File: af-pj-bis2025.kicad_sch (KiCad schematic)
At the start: 59 parts, among them IC1 ADS127L14IRSHT, IC2 OPA210IDBVR, IC3 REF6225IDGKR, IC4 TPS7A4700RGWR, IC5 TPS7A4700RGWR, U1 MIC5237-5.0YU, U2 ALD114904ASAL, U3 OPA380AID, U4 OPA380AID

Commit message: ADC追加
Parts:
- removed C1, C3, C8, C9: 3.18nF, symbol Device:C
- removed C4, C5: C, symbol Device:C
- removed IC1: ADS127L14IRSHT, QFN40P700X700X100-57N-D, symbol SamacSys_Parts:ADS127L14IRSHT
- removed IC2: OPA210IDBVR, SOT95P280X145-5N, symbol SamacSys_Parts:OPA210IDBVR
- removed IC3: REF6225IDGKR, SOP65P490X110-8N, symbol SamacSys_Parts:REF6225IDGKR
- removed IC4, IC5: TPS7A4700RGWR, QFN65P500X500X100-21N-D, symbol SamacSys_Parts:TPS7A4700RGWR
- removed R10: 0.047, symbol Device:R
- removed R11, R13, R14, R17, R18, R9: 0, symbol Device:R
- removed R12, R16: 0.1, symbol Device:R
- removed R15, R7: 100k, symbol Device:R
- removed R3, R4: R, symbol Device:R
- removed R5: 1.00k, symbol Device:R
- removed R6: 37.4, symbol Device:R
- removed R8: 120k, symbol Device:R
- removed Re1, Re2, Re3, Re4: 50kΩ, symbol Device:R
- removed U1: MIC5237-5.0YU, TO-263-3_MCL, symbol MIC5237-5.0YU:MIC5237-5.0YU
- removed U2: ALD114904ASAL, 8-SOIC_ALD, symbol ALD114904ASAL:ALD114904ASAL
- removed U3, U4: OPA380AID, D8, symbol OPA380:OPA380AID
- added C29: 1n, symbol Device:C
- added C30, C35, C36: 0.1u, symbol Device:C
- added C31, C32: 270p, symbol Device:C
- added C33: 22n, symbol Device:C
- added C34: 3.18n, symbol Device:C
- added Re10, Re20, Re21, Re24, Re25, Re7, Re8, Re9: 1.2k, symbol Device:R
- added Re11, Re12, Re26, Re27: 5, symbol Device:R
- added Re13, Re14, Re28, Re29: 10, symbol Device:R
- added Re15, Re16, Re17, Re18, Re19: 47, symbol Device:R
- added Re22, Re23, Re5, Re6: 330, symbol Device:R
- added Re30, Re32: 50k, symbol Device:R
- added Re31, Re33: 50k_throughhole, symbol Device:R
- added U1: MIC5237-5.0YU, TO-263-3_MCL, symbol pj-bis2025:MIC5237-5.0YU
- added U10, U7: THS4552IPWR, PW0016A_N, symbol Triac_Thyristor:THS4552IPWR
- added U11: OPA2380AIDGKR, DGK8, symbol pj-bis2025:OPA2380AIDGKR
- added U12: ALD114904APAL, 8-PDIP_ALD, symbol pj-bis2025:ALD114904APAL
- added U5: ADS1220IPW, PW16, symbol Triac_Thyristor:ADS1220IPW
- added U6: UA78L06ACPK, PK0003A_N, symbol Triac_Thyristor:UA78L06ACPK
- added U8: REF5050IDR, D8, symbol Triac_Thyristor:REF5050IDR
- added U9: LT1991ACMS-TRPBF, MSOP-10_MS_LIT, symbol Triac_Thyristor:LT1991ACMS-TRPBF
- C10: value 1u -> 470p
- C11: value 0.033u -> 270p
- C12: value 100 n -> 270p
- C13: value 10u -> 1n
- C14: value 1u -> 22n
- C15: value 47u -> 0.1u
- C16, C17: value 10u -> 0.1u
- C18: value 1u -> 0.1u
- C19: value 22u -> 0.1u
- C20: value 10u -> 3.18n
- C21: value 1u -> 3.18n
- C22: value 22u -> 3.18n
- C23: value C -> 0.33u
- C24, C26, C27: value C -> 0.1u
- C25: value C -> 1u
- C28: value C -> 470p
- R1: value 1.00 k -> 100k
- R2: value 4.99k -> 100k
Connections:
- net 5V is gone; now on net AVDD_5V: C6.1
- net IOVDD is gone; now on net DC_9V: C23.1
- net REFP is gone; now on net AVSS: C26.2
- net VCOM is gone; now on an unnamed net: C13.1
- net AVSS: now also C15.2, C17.1, C18.1, C19.1, C2.2, C21.1, C22.1, C23.2, C27.1, C6.2, C7.2, C30.1, C35.1, C36.1, Re21.1, Re8.1, U1.2 (GND), U1.4, U10.12 (VS-), U11.4 (V-), U12.4 (S12), U12.5 (V-), U5.5 (AVSS), U5.8 (REFN0), U6.2 (COMMON), U7.16 (VS-), U8.4 (GND), U9.3 (P9), U9.4 (VEE); no longer C10.2, C12.1, C13.2, C14.2, C16.2, C26.1, C27.2
- net GND: now also U5.3 (CLK); no longer C17.2, C18.2, C2.2, C20.2, C21.2, C23.2, C28.2, C6.2, C7.2
- net OUT1: now also C22.2, Re31.1, Re32.2, Re7.1
- net OUT2: now also C21.2, Re20.1, Re30.2, Re33.1
- net AIN1P: now reaches C14.1
- net AIN1P: now also Re14.2, U5.11 (AIN0/REFP1)
- net at C28.1: now also Re21.2, Re23.1, Re25.1
- net at C19.2: now also R1.2, U11.3 (INA+)
- net at C10.1: now also Re10.1, Re6.1, Re8.2; no longer R1.2
- net at R2.2: now also C35.2, U11.5 (INB+)
- net at C11.1: now also Re12.1, U7.14 (VOUT1+)
- net at C11.2: now also Re6.2, U7.3 (VIN1-); no longer R2.1
- net +2V5 renamed AVDD_5V
- net AVDD_5V: now also C17.2, C18.2, C36.2, U1.3 (OUT), U10.5 (PD2_N), U10.9 (VS2+), U11.8 (V+), U5.12 (AVDD), U7.1 (PD1_N), U7.13 (VS1+)
- net +6V: no longer names the net of C20.1
- net +6V: now also Re32.1, U11.1 (OUTA); no longer C17.1
- net +9V renamed DC_9V
- net DC_9V: now also U1.1 (IN), U6.3 (INPUT)
- removed net AVDD: C12.2, C16.1, C24.1, C25.1
- net VCM renamed VREF_0.5V
- net VREF_0.5V: now also R2.1, U9.10 (M1), U9.6 (OUT), U9.8 (M9), U9.9 (M3)
- new net: C10.2, Re5.1, Re7.2, Re9.1
- new net: C12.2, C13.2, Re5.2, U7.2 (VIN1+)
- new net: C27.2, U7.4 (VOCM1)
- new net: Re10.2, Re12.2, Re14.1
- new net: Re17.2, U5.16 (DIN)
- new net: C28.2, Re20.2, Re22.1, Re24.1
- new net: C32.1, Re27.1, U10.10 (VOUT2+)
- new net: Re25.2, Re27.2, Re29.1
- new net: Re18.1, U5.15 (DOUT/*DRDY)
- new net: C29.2, C31.2, Re22.2, U10.6 (VIN2+)
- new net: Re24.2, Re26.2, Re28.1
- new net: Re15.2, U5.2 (*CS)
- new net: C25.1, U8.5 (TRIM/NR)
- new net: C31.1, Re26.1, U10.11 (VOUT2-)
- new net: C34.1, Re30.1, U11.7 (OUTB)
- new net: C30.2, U10.8 (VOCM2)
- new net: C29.1, C32.2, Re23.2, U10.7 (VIN2-)
- new net: C20.2, Re31.2, U11.2 (INA-), U12.3 (DN1)
- new net: Re11.2, Re13.1, Re9.2
- new net: C12.1, Re11.1, U7.15 (VOUT1-)
- new net: C34.2, Re33.2, U11.6 (INB-), U12.6 (DN2)
- new net: Re16.2, U5.1 (SCLK)
- new net: Re19.1, U5.14 (*DRDY)
- new net AIN1N: C14.2, Re13.2, U5.10 (AIN1)
- new net AIN2N: C33.2, Re28.2, U5.6 (AIN3/REFN1)
- new net AIN2P: C33.1, Re29.2, U5.7 (AIN2)
- new net AVDD_6.2V: C24.1, U6.1 (OUTPUT), U8.2 (VIN)
- new net AVDD_6V: C26.1, U9.7 (VCC)
- new net CS*: Re15.1
- new net DIN: Re17.1
- new net DOUT: Re18.2
- new net DRDY: Re19.2
- new net DVDD: C16.1, U5.13 (DVDD)
- new net DVSS: C16.2, U5.4 (DGND)
- new net GATE1: U12.2 (GN1)
- new net GATE2: U12.7 (GN2)
- new net SCLK: Re16.1
- new net VREF_5V: U5.9 (REFP0), U8.6 (VOUT), U9.1 (P1), U9.5 (REF)
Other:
- moved on the sheet: C2, C6, C7

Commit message: ERCを解消した1
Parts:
- removed U10, U7: THS4552IPWR, PW0016A_N, symbol Triac_Thyristor:THS4552IPWR
- added U2: THS4552IPWR, PW0016A_N, symbol pj-bis2025:THS4552IPWR
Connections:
- net AVDD_6V is gone; now on net AVDD_6.2V: C26.1, U9.7 (VCC)
- net AVDD_5V: now also U2.1 (PD1_N), U2.13 (VS1+), U2.5 (PD2_N), U2.9 (VS2+)
- net AVSS: now also U2.12 (VS-), U2.16 (VS-)
- net at C11.1, Re12.1: now also U2.14 (VOUT1+)
- net at C11.2, C13.1, Re6.2: now also U2.3 (VIN1-)
- net at C12.2, C13.2, Re5.2: now also U2.2 (VIN1+)
- net at C27.2: now also U2.4 (VOCM1)
- net at C32.1, Re27.1: now also U2.10 (VOUT2+)
- net at C29.2, C31.2, Re22.2: now also U2.6 (VIN2+)
- net at C31.1, Re26.1: now also U2.11 (VOUT2-)
- net at C30.2: now also U2.8 (VOCM2)
- net at C29.1, C32.2, Re23.2: now also U2.7 (VIN2-)
- net at C12.1, Re11.1: now also U2.15 (VOUT1-)
- no-connect marks 0 -> 1

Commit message: ERCエラー修正2
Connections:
- net GND is gone; now on net AVSS: U5.3 (CLK)
- no-connect marks 1 -> 7
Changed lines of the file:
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@@
 	)
 	(no_connect
+		(at -25.4 295.91)
+	)
+	(no_connect
+		(at 393.7 269.24)
+	)
+	(no_connect
+		(at 30.48 295.91)
+	)
+	(no_connect
+		(at 393.7 264.16)
+	)
+	(no_connect
+		(at 459.74 266.7)
+	)
+	(no_connect
 		(at 482.6 266.7)
 	)
+	(no_connect
+		(at 459.74 264.16)
+	)
 	(wire
 		(pts
@@
 		)
 	)
+	(label "AVSS"
+		(at 335.28 309.88 0)
+		(effects
+			(font
+				(size 1.27 1.27)
+			)
+			(justify left bottom)
+		)
+	)
 	(label "AVDD_6.2V"
 		(at 542.29 271.78 0)
@@
 					(unit 1)
 				)
-			)
-		)
-	)
-	(symbol
-		(lib_id "power:GND")
-		(at 335.28 309.88 0)
-		(unit 1)
-		(exclude_from_sim no)
-		(in_bom yes)
-		(on_board yes)
-		(dnp no)
-		(fields_autoplaced yes)
-		(property "Reference" "#PWR025"
-			(at 335.28 316.23 0)
-			(effects
-				(font
-					(size 1.27 1.27)
-				)
-				(hide yes)
-			)
-		)
-		(property "Value" "GND"
-			(at 335.28 314.96 0)
-			(effects
-				(font
-					(size 1.27 1.27)
-				)
-			)
-		)
-		(property "Footprint" ""
-			(at 335.28 309.88 0)
-			(effects
-				(font
-					(size 1.27 1.27)
-				)
-				(hide yes)
-			)
-		)
-		(property "Datasheet" ""
-			(at 335.28 309.88 0)
-			(effects
-				(font
-					(size 1.27 1.27)
-				)
-				(hide yes)
-			)
-		)
-		(property "Description" "Power symbol creates a global label with name \"GND\" , ground"
-			(at 335.28 309.88 0)
-			(effects
-				(font
-					(size 1.27 1.27)
-				)
-				(hide yes)
-			)
-		)
-		(pin "1"
-		)
-		(instances
-			(project "af-pj-bis2025"
-				(path "/0c43c024-04be-42a3-97bf-885833c3aea8"
-					(reference "#PWR025")
-					(unit 1)
-				)

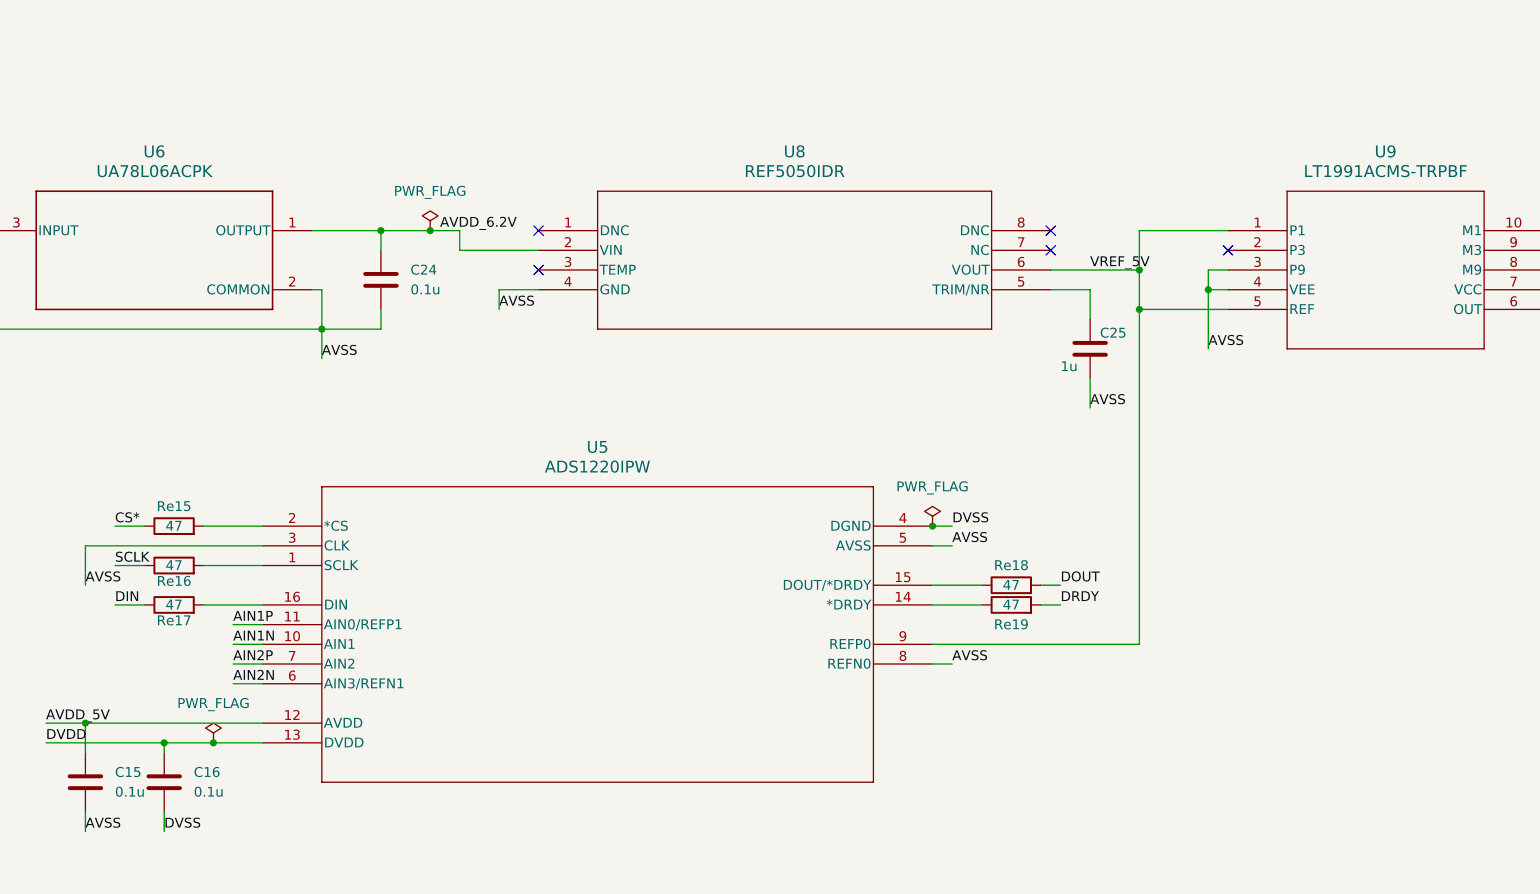
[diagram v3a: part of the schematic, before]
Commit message: パスコンを追加
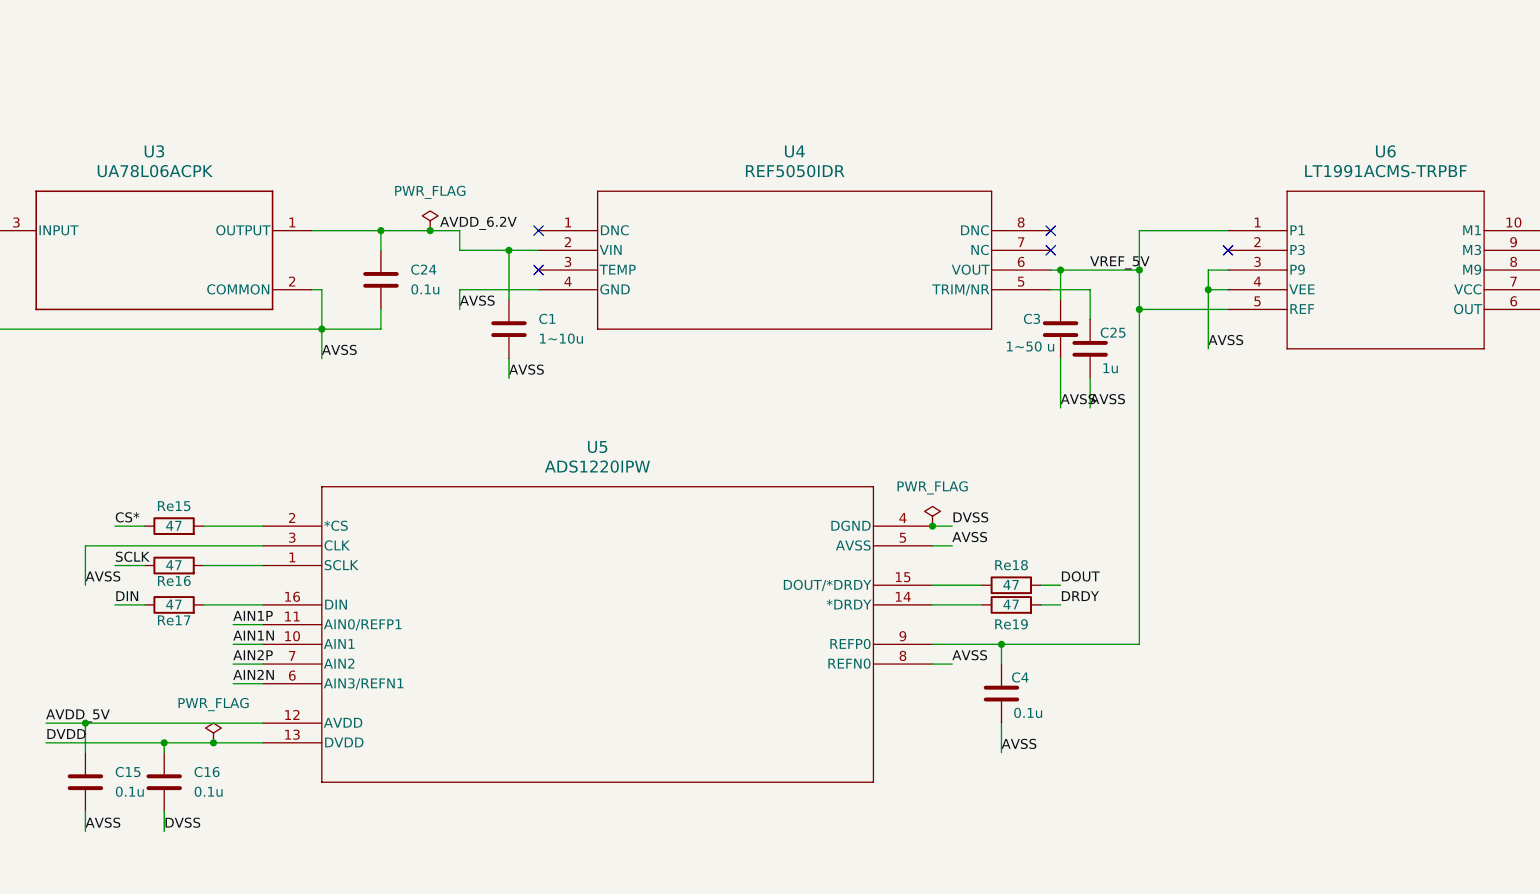
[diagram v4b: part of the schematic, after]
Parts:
- removed U5: ADS1220IPW, PW16, symbol Triac_Thyristor:ADS1220IPW
- removed U6: UA78L06ACPK, PK0003A_N, symbol Triac_Thyristor:UA78L06ACPK
- removed U8: REF5050IDR, D8, symbol Triac_Thyristor:REF5050IDR
- removed U9: LT1991ACMS-TRPBF, MSOP-10_MS_LIT, symbol Triac_Thyristor:LT1991ACMS-TRPBF
- added C1: 1~10u, symbol Device:C
- added C3: 1~50 u, symbol Device:C
- added C4: 0.1u, symbol Device:C
- added U3: UA78L06ACPK, PK0003A_N, symbol pj-bis2025:UA78L06ACPK
- added U4: REF5050IDR, D8, symbol pj-bis2025:REF5050IDR
- added U5: ADS1220IPW, PW16, symbol pj-bis2025:ADS1220IPW
- added U6: LT1991ACMS-TRPBF, MSOP-10_MS_LIT, symbol pj-bis2025:LT1991ACMS-TRPBF
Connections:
- net AIN1N: now also U5.10 (AIN1)
- net AIN1P: now also U5.11 (AIN0/REFP1)
- net AIN2N: now also U5.6 (AIN3/REFN1)
- net AIN2P: now also U5.7 (AIN2)
- net AVDD_5V: now also U5.12 (AVDD)
- net AVDD_6.2V: now also C1.1, U3.1 (OUTPUT), U4.2 (VIN), U6.7 (VCC)
- net AVSS: now also C1.2, C3.2, C4.2, U3.2 (COMMON), U4.4 (GND), U5.3 (CLK), U5.5 (AVSS), U5.8 (REFN0), U6.3 (P9), U6.4 (VEE)
- net DC_9V: now also U3.3 (INPUT)
- net DVDD: now also U5.13 (DVDD)
- net DVSS: now also U5.4 (DGND)
- net VREF_0.5V: now also U6.10 (M1), U6.6 (OUT), U6.8 (M9), U6.9 (M3)
- net VREF_5V: now also C3.1, C4.1, U4.6 (VOUT), U5.9 (REFP0), U6.1 (P1), U6.5 (REF)
- net at Re17.2: now also U5.16 (DIN)
- net at Re18.1: now also U5.15 (DOUT/*DRDY)
- net at Re15.2: now also U5.2 (*CS)
- net at C25.1: now also U4.5 (TRIM/NR)
- net at Re16.2: now also U5.1 (SCLK)
- net at Re19.1: now also U5.14 (*DRDY)

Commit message: Uのフットプリント割り当て完了
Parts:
- C6: footprint TCJB_AVX -> (none)
- U1: footprint TO-263-3_MCL -> pj-bis2025:MIC5237-TO-263-3_MCL-M
- U11: footprint DGK8 -> pj-bis2025:OPA2380-DGK8-M
- U12: footprint 8-PDIP_ALD -> pj-bis2025:ALD114904APAL-8-PDIP_ALD
- U2: footprint PW0016A_N -> pj-bis2025:THS4552-PW0016A_M
- U3: footprint PK0003A_N -> pj-bis2025:UA78L06ACPK-PK0003A_M
- U4: footprint D8 -> pj-bis2025:REF5050-D8-M
- U5: footprint PW16 -> pj-bis2025:ADS1220-PW16-M
- U6: footprint MSOP-10_MS_LIT -> pj-bis2025:LT1991-MSOP-10_MS_LIT-M
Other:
- moved on the sheet: C1, C10, C11, C12, C13, C14, C15, C16, C17, C18, C19, C2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

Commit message: アノテーション
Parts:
- renumbered C6 to C1, C35 to C10, C12 to C11, C17 to C12, C10 to C13, C13 to C14, C14 to C15, C27 to C16, C11 to C17, C31 to C18, C18 to C19, C28 to C20, C29 to C21, C33 to C22, C30 to C23, C32 to C24, C23 to C25, C24 to C26, C1 to C27, C3 to C28, C26 to C29, C7 to C3, C25 to C30, C4 to C31, C15 to C32, C16 to C33, C20 to C4, C34 to C5, C19 to C6, C22 to C7, C36 to C8, C21 to C9, Re31 to Re1, Re12 to Re10, Re14 to Re11, Re8 to Re12, Re6 to Re13, Re10 to Re14, Re24 to Re15, Re20 to Re16, Re22 to Re17, Re26 to Re18, Re28 to Re19, Re33 to Re2, Re27 to Re20, Re29 to Re21, Re21 to Re22, Re25 to Re24, Re15 to Re25, Re16 to Re26, Re18 to Re27, Re17 to Re28, Re19 to Re29, Re32 to Re3, Re30 to Re4, Re9 to Re5, Re7 to Re6, Re5 to Re7, Re11 to Re8, Re13 to Re9, U12 to U2, U11 to U3, U2 to U4, U4 to U5, U3 to U7, U5 to U8
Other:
- moved on the sheet: C25, C26, C27, C28, C29, C30, C31, C32, C33, Re25, Re26, Re27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
